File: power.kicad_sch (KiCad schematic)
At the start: 47 parts, among them CN14 DF40C-30DP-0.4V, J2 TYPE-C16PIN, J21 Molex_53047-0310, Q5 CSD17575Q3A, Q6 CSD17575Q3A, Q7 CSD17575Q3A, Q8 CSD17575Q3A, U2 CH224K, U3 BQ25792RQMR, U4 AP2112K-3.3TRG1, U5 AP2112K-1.8TRG1, U6 LP8556SQ-E09/NOPB, U9 TPS61088RHLR

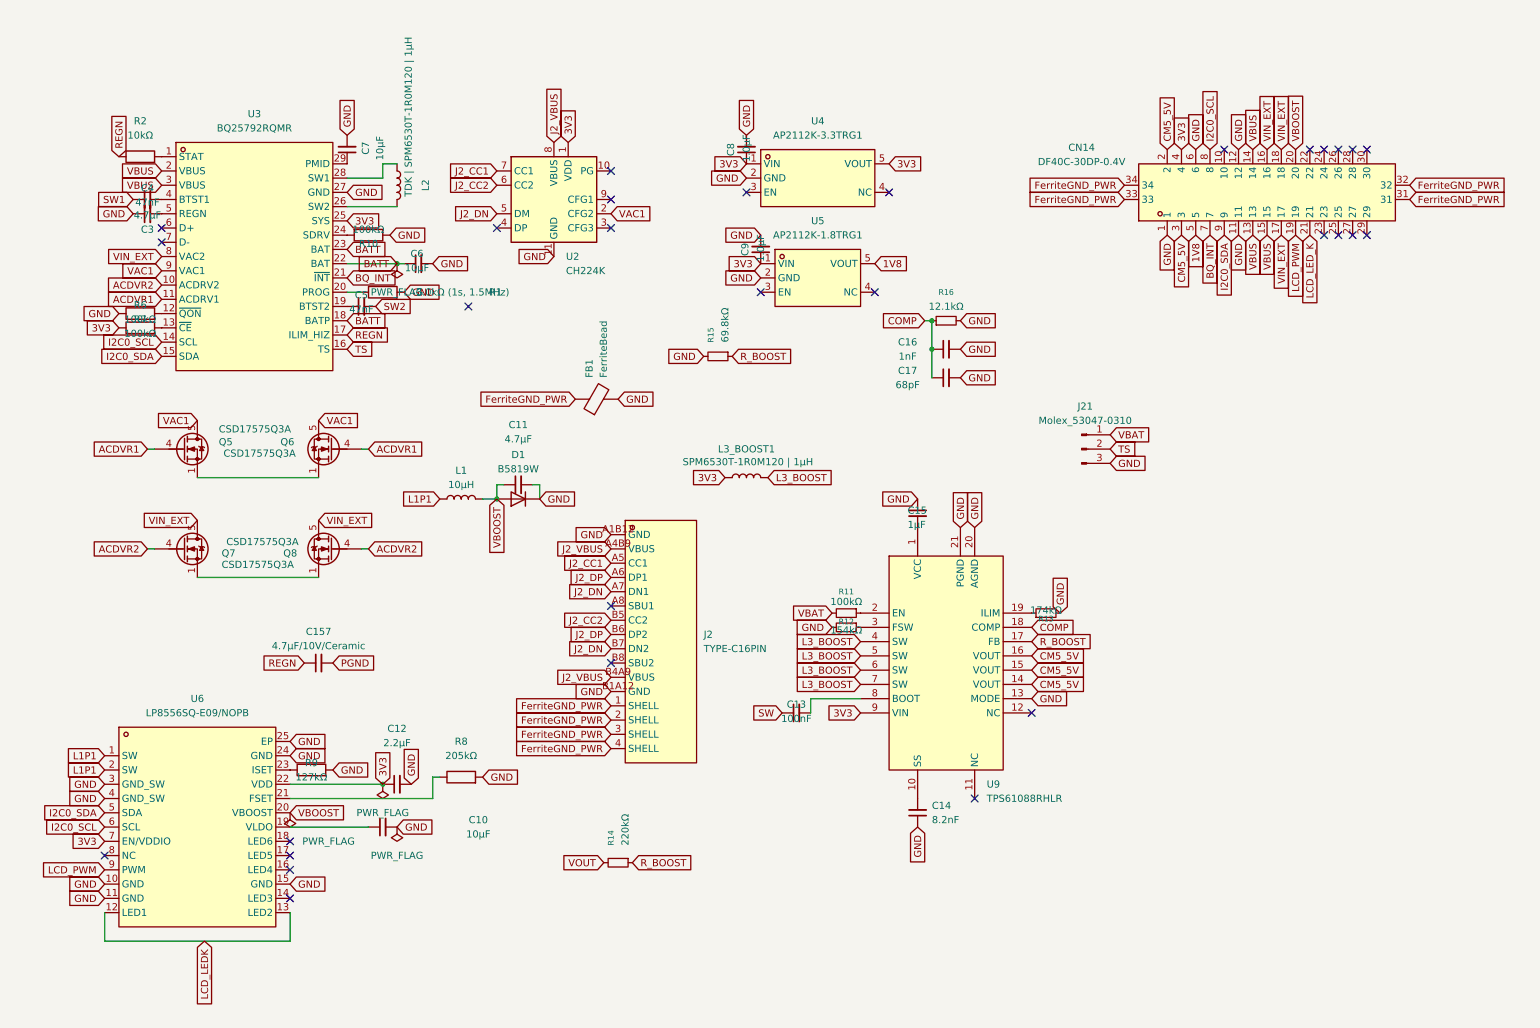
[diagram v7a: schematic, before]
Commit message: imported footprints and 3d models, replaced obsolete components, finished schematic audit, wired new usb hub and flash chip + more, removed stale nets
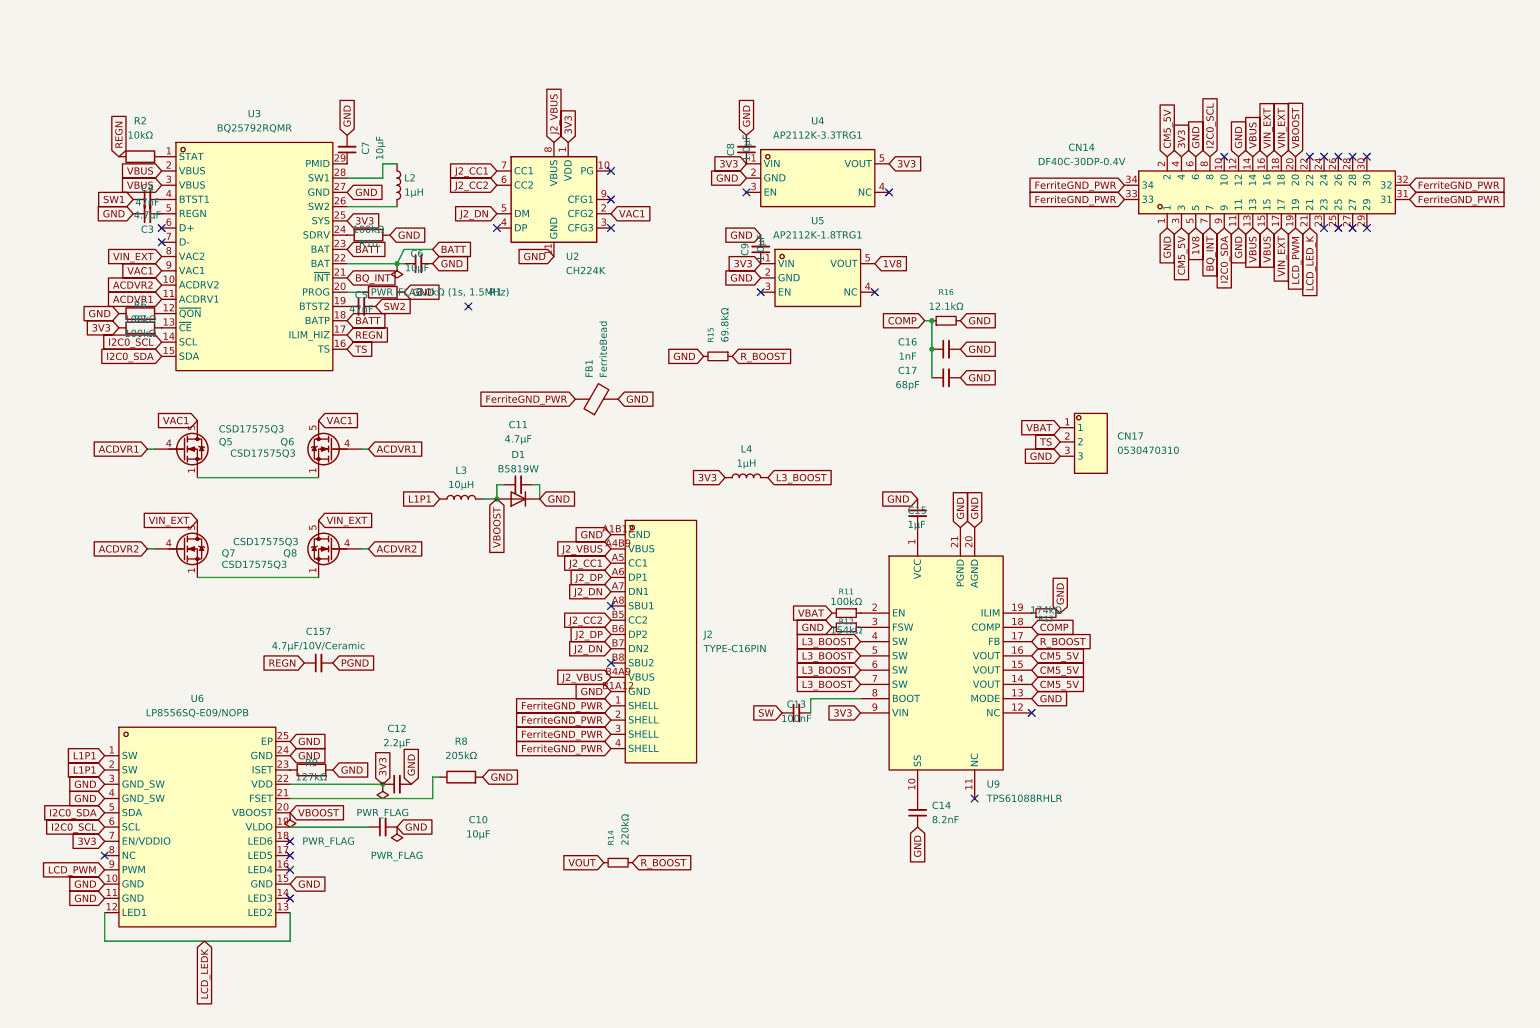
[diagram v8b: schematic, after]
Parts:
- removed J21: Molex_53047-0310, symbol Connector:Conn_01x03_Pin
- removed L1: 10µH, symbol Device:L
- removed L3_BOOST1: SPM6530T-1R0M120 | 1µH, symbol Device:L
- added CN17: 0530470310, slate113:CONN-TH_0530470310, symbol slate113:0530470310
- added L3: 10µH, symbol Device:L
- added L4: 1µH, symbol Device:L
- C11, C157, C3: LCSC Part C49326377 -> C77045; MPN 0603X5R475K160NT -> GRM188R61C475KE11D; Manufacturer Samsung Electro-Mechanics -> Murata Electronics
- C12: LCSC Part C49326370 -> C7432769; MPN 0603X5R225K350NT -> HGC0603R5225K500NTHJ; Manufacturer Samsung Electro-Mechanics -> Chinocera
- C14: footprint (none) -> Capacitor_SMD:C_0603_1608Metric
- C15, C8, C9: LCSC Part C49326357 -> C5673; MPN 0603X5R105K160NT -> CL10A105KA8NNNC
- D1: footprint (none) -> Diode_SMD:D_SOD-123
- L2: value TDK | SPM6530T-1R0M120 | 1µH -> 1µH; DigiKey Part 445-3880-2-ND -> (none); Manufacturer (none) -> TDK
- Q5, Q6, Q7, Q8: value CSD17575Q3A -> CSD17575Q3; footprint Package_TO_SOT_SMD:TDSON-8-1 -> slate113:VSON-CLIP-8_L3.3-W3.3-P0.65-BL; Manufacturer LCSC -> Texas Instruments
- R2: LCSC Part C25804 -> C840630; MPN 0603WAF1002T5E -> CR0603-FX-1002ELF; Manufacturer Yageo -> Bourns
- R9: DigiKey Part (none) -> 311-127KHRCT-ND; LCSC Part C22869 -> (none); MPN 0603WAF1273T5E -> RC0603FR-07127KL
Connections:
- net 3V3: now also L4.1
- net GND: now also CN17.3
- net L1P1: now also L3.1
- net L3_BOOST: now also L4.2
- net TS: now also CN17.2
- net VBAT: now also CN17.1
- net VBOOST: now also L3.2
